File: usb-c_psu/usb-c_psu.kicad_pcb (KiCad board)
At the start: 2 copper layers, 24.3 x 92.3 mm, 12 parts, among them J1 Conn_01x01_Socket, J10 Conn_01x01_Socket, J11 Conn_01x02_Socket, J2 Conn_01x01_Socket, J3 Conn_01x01_Socket, J4 Conn_01x01_Socket, J5 Conn_01x01_Socket, J6 Conn_01x01_Socket, J7 Conn_01x01_Socket, J8 Conn_01x01_Socket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

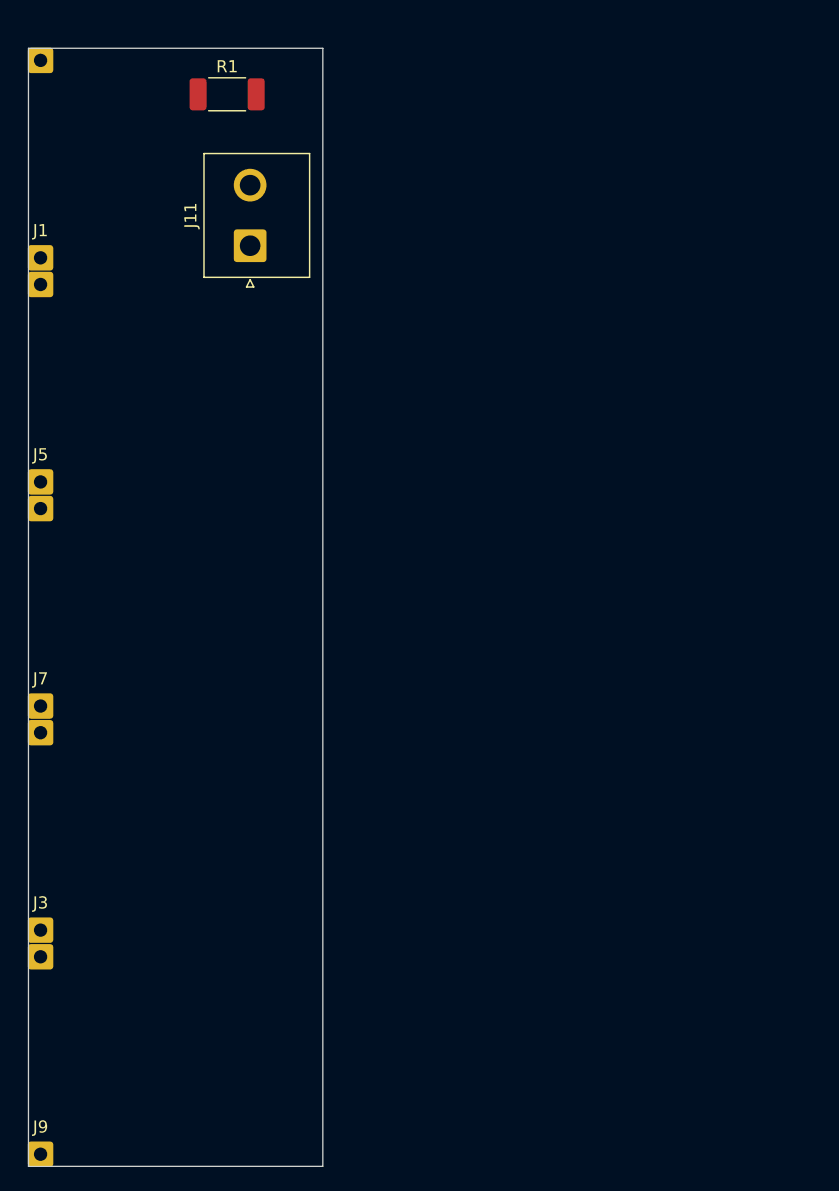
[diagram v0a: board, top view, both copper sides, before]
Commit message: update connector footprints
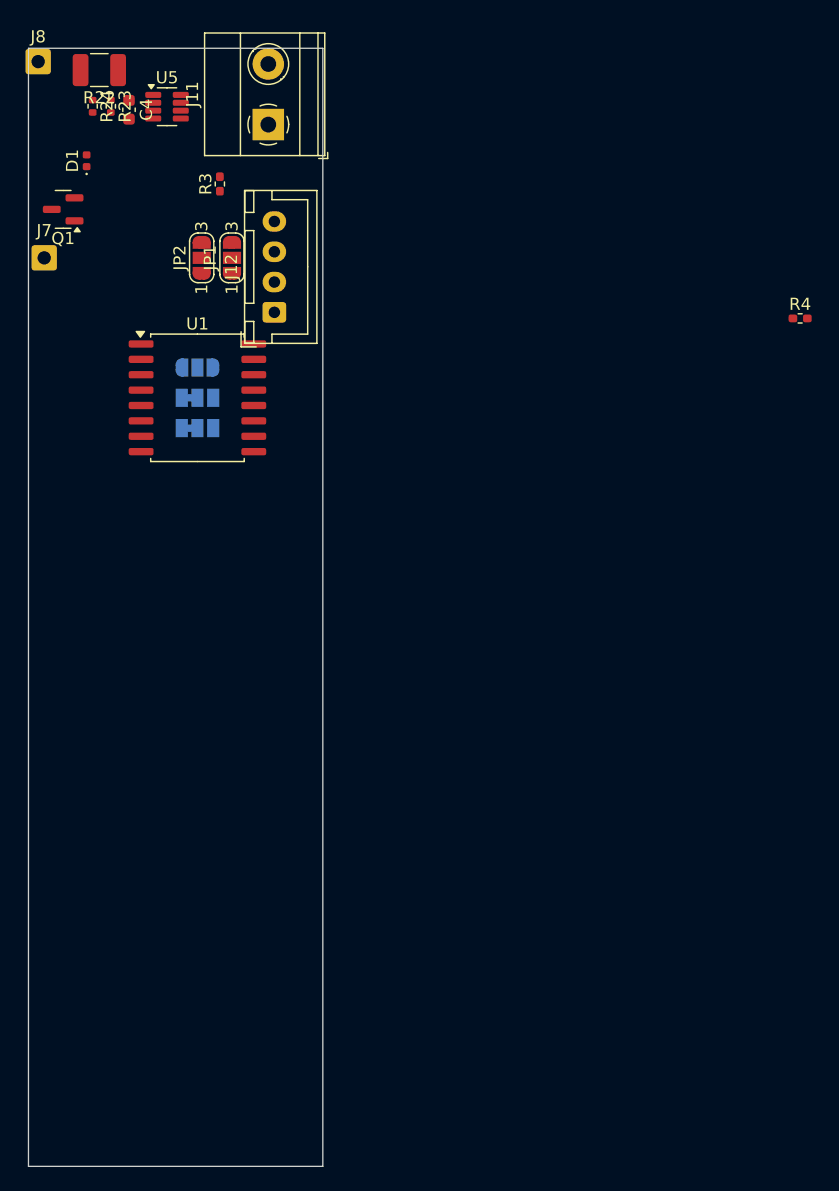
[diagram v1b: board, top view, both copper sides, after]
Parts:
- removed J1, J10, J2, J3, J4, J5, J6, J9: Conn_01x01_Socket, Connector_Wire:SolderWire-0.5sqmm_1x01_D0.9mm_OD2.1mm
- removed R1: R, Resistor_SMD:R_2010_5025Metric_Pad1.40x2.65mm_HandSolder
- added C4: 1uF, Capacitor_SMD:C_0603_1608Metric, F.Cu at (142.0, 41.3)
- added D1: LED, LED_SMD:LED_0402_1005Metric, F.Cu at (138.5, 45.5)
- added J12: Conn_01x04, Connector_JST:JST_XH_B4B-XH-A_1x04_P2.50mm_Vertical, F.Cu at (154.0, 58.0)
- added JP1: SolderJumper_3_Open, Jumper:SolderJumper-3_P1.3mm_Open_RoundedPad1.0x1.5mm_NumberLabels, F.Cu at (150.5, 53.5)
- added JP2: SolderJumper_3_Open, Jumper:SolderJumper-3_P1.3mm_Open_RoundedPad1.0x1.5mm_NumberLabels, F.Cu at (148.0, 53.5)
- added JP3: A0, Jumper:SolderJumper-3_P1.3mm_Open_RoundedPad1.0x1.5mm_NumberLabels, B.Cu at (147.7, 62.6)
- added JP4: A2, Jumper:SolderJumper-3_P1.3mm_Bridged12_Pad1.0x1.5mm_NumberLabels, B.Cu at (147.7, 65.1)
- added JP5: A1, Jumper:SolderJumper-3_P1.3mm_Bridged12_Pad1.0x1.5mm_NumberLabels, B.Cu at (147.7, 67.6)
- added Q1: DMN3404L, Package_TO_SOT_SMD:SOT-23, F.Cu at (136.6, 49.5)
- added R22: 0R1, Resistor_SMD:R_1210_3225Metric_Pad1.30x2.65mm_HandSolder, F.Cu at (139.6, 38.0)
- added R23: R10, Resistor_SMD:R_0402_1005Metric, F.Cu at (140.5, 41.0)
- added R24: R10, Resistor_SMD:R_0402_1005Metric, F.Cu at (139.0, 41.0)
- added R3: R, Resistor_SMD:R_0402_1005Metric_Pad0.72x0.64mm_HandSolder, F.Cu at (149.5, 47.4)
- added R4: R, Resistor_SMD:R_0402_1005Metric_Pad0.72x0.64mm_HandSolder, F.Cu at (197.4, 58.5)
- added U1: PCF8574, Package_SO:SOIC-16W_7.5x10.3mm_P1.27mm, F.Cu at (147.7, 65.1)
- added U5: INA219AxDCN, Package_TO_SOT_SMD:SOT-23-8, F.Cu at (145.1, 41.0)
- J11: value Conn_01x02_Socket -> 24V_IN; footprint Connector_JST:JST_NV_B02P-NV_1x02_P5.00mm_Vertical -> TerminalBlock_Phoenix:TerminalBlock_Phoenix_MKDS-1,5-2_1x02_P5.00mm_Horizontal
- J7: value Conn_01x01_Socket -> CHAN0-
- J8: value Conn_01x01_Socket -> CHAN0+; moved to F.Cu
- moved J7 37.0 mm to (135.0, 53.5)
- moved J8 36.7 mm to (134.5, 37.5), turned to 0 degrees
- moved J11 10.1 mm to (153.5, 42.5)
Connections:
- J11 pad 1: Net-(J11-Pin_1) -> +24V
- J11 pad 2: GND -> GNDPWR
- J7 pad 1: GND -> Net-(J7-Pin_1)
- J8 pad 1: PWR -> Net-(J8-Pin_1)
